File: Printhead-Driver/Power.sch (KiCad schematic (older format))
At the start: 50 parts, among them J3 24V Power In, J4 ADC Select1, U10 MC34063AD, U11 ADC121C021CIMM, U9 MCA1101-5-3

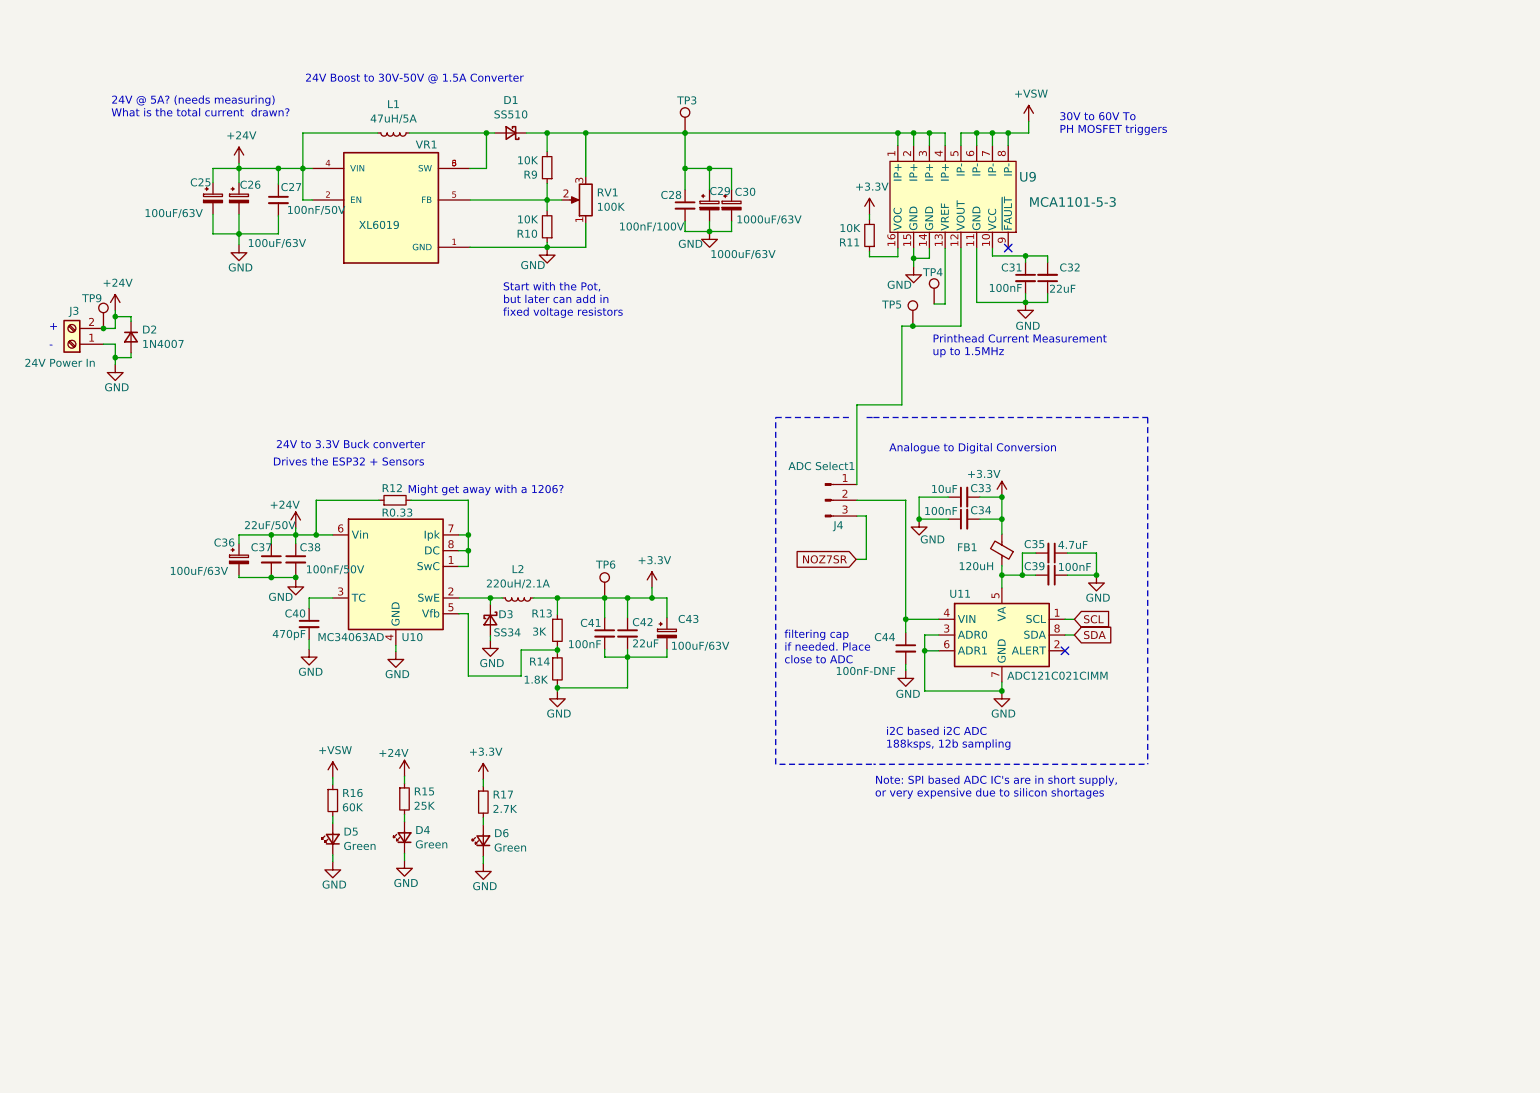
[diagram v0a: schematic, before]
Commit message: final PCB KiCAD design files for V0.5 as sent off for manufacture at JLCPCB 2022-03-22
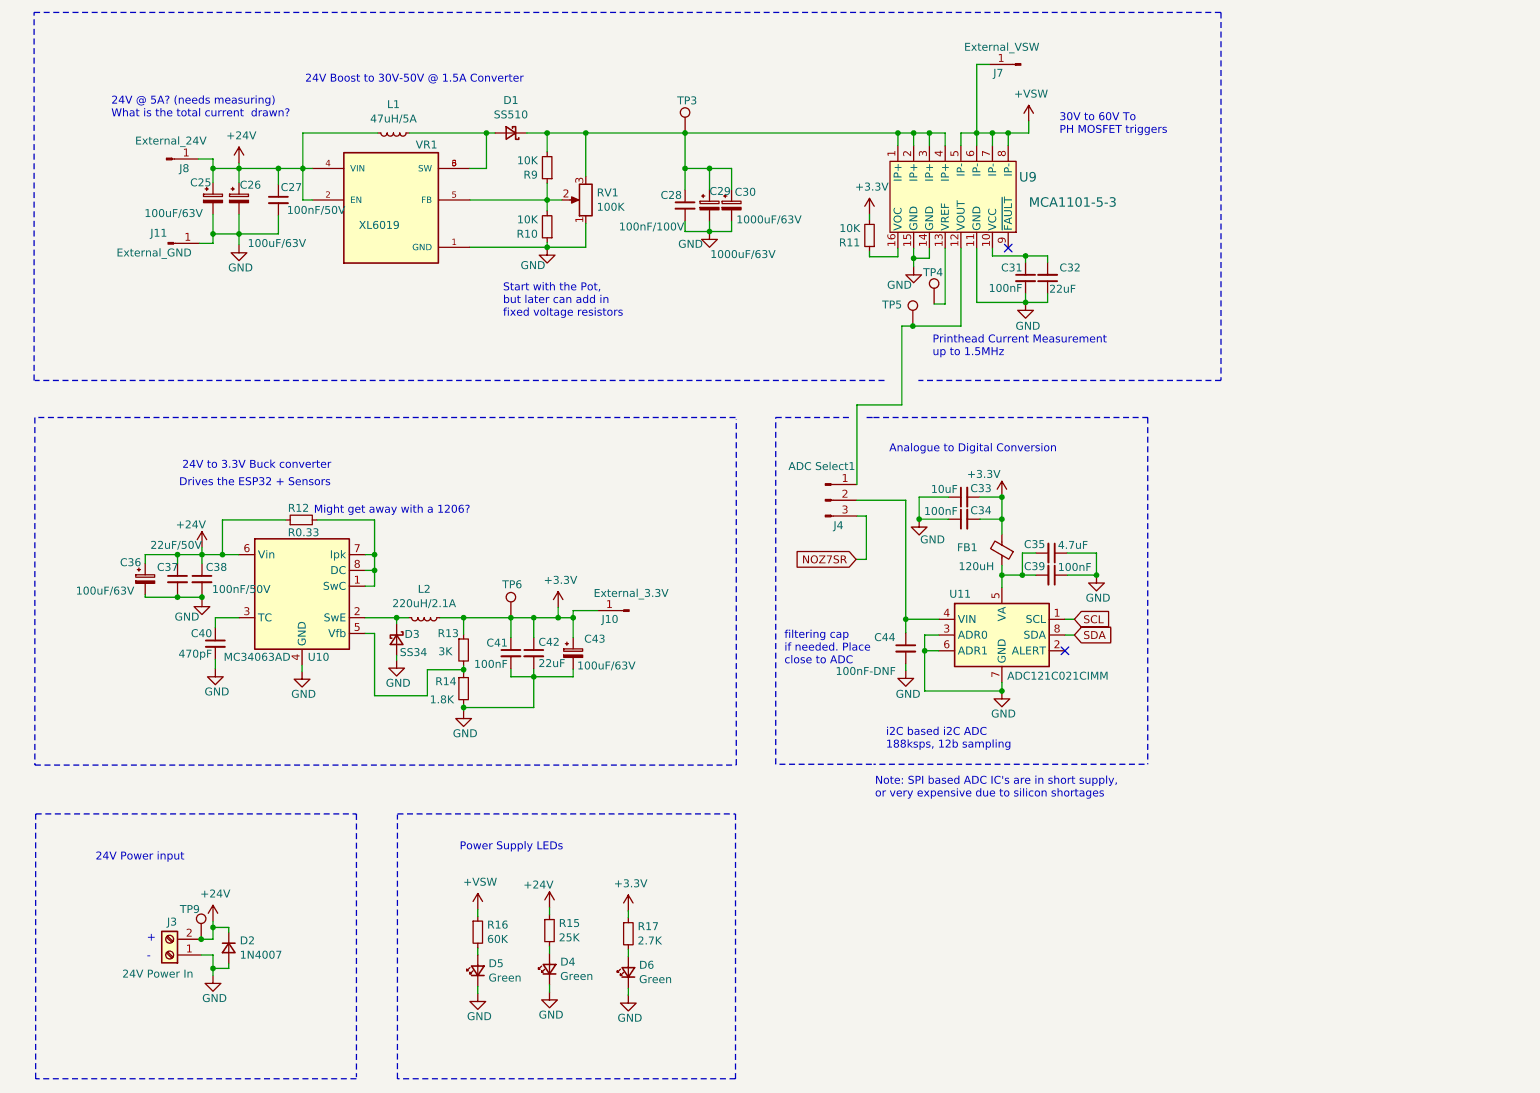
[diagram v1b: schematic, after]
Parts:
- added J10: External_3.3V, Connector_PinHeader_2.54mm:PinHeader_1x01_P2.54mm_Vertical, symbol Connector:Conn_01x01_Male
- added J11: External_GND, Connector_PinHeader_2.54mm:PinHeader_1x01_P2.54mm_Vertical, symbol Connector:Conn_01x01_Male
- added J7: External_VSW, Connector_PinHeader_2.54mm:PinHeader_1x01_P2.54mm_Vertical, symbol Connector:Conn_01x01_Male
- added J8: External_24V, Connector_PinHeader_2.54mm:PinHeader_1x01_P2.54mm_Vertical, symbol Connector:Conn_01x01_Male
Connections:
- net +24V: now also J8.1 (Pin_1)
- net +3V3: now also J10.1 (Pin_1)
- net +VSW: now also J7.1 (Pin_1)
- net GND: now also J11.1 (Pin_1)
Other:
- note added: "24V Power input"
- note added: "Power Supply LEDs"
- moved on the sheet: C36, C37, C38, C40, C41, C42, C43, D2, D3, D4, D5, D6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

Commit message: Adding in version 0.7 KiACD design files
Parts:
- removed C30: 1000uF/63V, Capacitor_THT:CP_Radial_D16.0mm_P7.50mm, symbol Device:CP_Small
- removed C31, C39: 100nF, Capacitor_SMD:C_0603_1608Metric, symbol Device:C_Small
- removed C32: 22uF, Capacitor_SMD:C_0603_1608Metric, symbol Device:C_Small
- removed D2: 1N4007, Diode_SMD:D_SMA, symbol Device:D_Small
- removed FB1: 120uH, Resistor_SMD:R_0805_2012Metric, symbol Device:Ferrite_Bead_Small
- removed J10: External_3.3V, Connector_PinHeader_2.54mm:PinHeader_1x01_P2.54mm_Vertical, symbol Connector:Conn_01x01_Male
- removed J11: External_GND, Connector_PinHeader_2.54mm:PinHeader_1x01_P2.54mm_Vertical, symbol Connector:Conn_01x01_Male
- removed J4: ADC Select1, Connector_PinHeader_2.54mm:PinHeader_1x03_P2.54mm_Vertical, symbol Connector:Conn_01x03_Male
- removed J7: External_VSW, Connector_PinHeader_2.54mm:PinHeader_1x01_P2.54mm_Vertical, symbol Connector:Conn_01x01_Male
- removed J8: External_24V, Connector_PinHeader_2.54mm:PinHeader_1x01_P2.54mm_Vertical, symbol Connector:Conn_01x01_Male
- removed TP4, TP5: TestPoint, TestPoint:TestPoint_THTPad_1.5x1.5mm_Drill0.7mm, symbol Connector:TestPoint
- removed U11: ADC121C021CIMM, Package_SO:MSOP-8_3x3mm_P0.65mm, symbol Analog_ADC:ADC121C021CIMM
- removed U9: MCA1101-5-3, Package_SO:SOIC-16W_7.5x10.3mm_P1.27mm, symbol Pauls_Symbol_Library:MCA1101-5-3
- added C36, C37, C51, C53, C55, C65, C67: 100nF, Capacitor_SMD:C_0603_1608Metric, symbol Device:C_Small
- added C38: 10nF/DNF, Capacitor_SMD:C_0603_1608Metric, symbol Device:C_Small
- added C45, C46, C47, C48, C49, C50: 1nF/DNF, Capacitor_SMD:C_0603_1608Metric, symbol Device:C_Small
- added C52, C54, C56, C66: 10uF, Capacitor_SMD:C_0603_1608Metric, symbol Device:C_Small
- added C61: 100nF 10V, Capacitor_SMD:C_0603_1608Metric, symbol Device:C_Small
- added C68: 1uF, Capacitor_SMD:C_0603_1608Metric, symbol Device:C_Small
- added D3: 12V, Diode_SMD:D_SOD-123, symbol Device:D_Zener_Small
- added D6: Green, Diode_SMD:D_0603_1608Metric, symbol Device:LED_Small
- added F1: 5A, Pauls_KiCAD_Libraries:Fuse_Holder_1808_10.0mmx5mm, symbol Device:Fuse_Small
- added L1, L4: 1uH 1.4A, Inductor_SMD:L_0805_2012Metric, symbol Device:L_Small
- added L3: 1uH 4A, Inductor_SMD:L_Taiyo-Yuden_MD-5050, symbol Device:L_Small
- added L6: 1uH/1.4A, Inductor_SMD:L_0805_2012Metric, symbol Device:L_Small
- added Q1, Q2: RU30L30, Pauls_KiCAD_Libraries:PDFN3333, symbol Pauls_Symbol_Library:RU30L30
- added R18: 4.7K, Resistor_SMD:R_0603_1608Metric, symbol Device:R_Small
- added R20, R24: 100k, Resistor_SMD:R_0603_1608Metric, symbol Device:R_Small
- added R21: 130, Resistor_SMD:R_0603_1608Metric, symbol Device:R_Small
- added R22: 150R, Resistor_SMD:R_0603_1608Metric, symbol Device:R_Small
- added R23: 100*, Resistor_SMD:R_0603_1608Metric, symbol Device:R_Small
- added R9: 100K, Resistor_SMD:R_0603_1608Metric, symbol Device:R_Small
- added SW1: PWR SW C128955, Pauls_KiCAD_Libraries:SW_SMD_SPDT_PCM12_7.8x3.8, symbol Pauls_Symbol_Library:Switch_Slide-3pole
- added TP10, TP11, TP12, TP6, TP8: TestPoint, TestPoint:TestPoint_THTPad_1.5x1.5mm_Drill0.7mm, symbol Connector:TestPoint
- added U17: ADC128S102CIMTX, Package_SO:TSSOP-16_4.4x5mm_P0.65mm, symbol Pauls_Symbol_Library:ADC128S102CIMTX
- added U18: HE6550MPR, Package_TO_SOT_SMD:SOT-89-3, symbol Pauls_Symbol_Library:HE6550MPR
- added U20: XC6227C331MR, Package_TO_SOT_SMD:SOT-23-5, symbol Printhead-Driver-rescue:XC6227C331MR-Pauls_Symbol_Library
- added U21: LM4040DIM3X-5, Package_TO_SOT_SMD:SOT-23, symbol Reference_Voltage:LM4040DBZ-5
- C33: value 10uF -> 1uF
- C35: value 4.7uF -> 1uF
- C41: renamed from C27; value 100nF/50V -> 100nF/100V
- C44: value 100nF-DNF -> 1nF/DNF; Description (none) -> 16V Ceramic
- C58: renamed from C37; value 22uF/50V -> 22uF/35V; footprint Capacitor_SMD:C_0603_1608Metric -> Capacitor_SMD:C_1210_3225Metric
- C59: renamed from C38; value 100nF/50V -> 100nF/35V; footprint Capacitor_SMD:C_0603_1608Metric -> Capacitor_SMD:C_1206_3216Metric
- C62: renamed from C41; value 100nF -> 100nF 10V
- D4, D5: footprint LED_SMD:LED_0805_2012Metric -> Diode_SMD:D_0603_1608Metric
- D7: renamed from D6; footprint LED_SMD:LED_0805_2012Metric -> Diode_SMD:D_0603_1608Metric
- J3: footprint TerminalBlock:TerminalBlock_Altech_AK300-2_P5.00mm -> Pauls_KiCAD_Libraries:JST-XH-2P_SMD
- R10: renamed from R9; value 10K -> 10K-DNF
- R12: renamed from R10; value 10K -> 10K-DNF
- R13: renamed from R12; footprint Resistor_SMD:R_2512_6332Metric -> Resistor_SMD:R_1206_3216Metric
- R14: renamed from R13; value 3K -> 4.7K
- R15: renamed from R14; value 1.8K -> 1.0K
- R16: renamed from R15; value 25K -> 27K; footprint Resistor_SMD:R_0805_2012Metric -> Resistor_SMD:R_0603_1608Metric
- R17: renamed from R16; value 60K -> 62K; footprint Resistor_SMD:R_0805_2012Metric -> Resistor_SMD:R_0603_1608Metric
- R19: renamed from R17; footprint Resistor_SMD:R_0805_2012Metric -> Resistor_SMD:R_0603_1608Metric
- renumbered C25 to C39, C26 to C40, C28 to C42, C29 to C43, C36 to C57, C40 to C60, C42 to C63, C43 to C64, D3 to D2, L1 to L2, L2 to L5, TP3 to TP5, TP6 to TP7, U10 to U19
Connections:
- net +24V: now also Q2.3 (D); no longer J3.2 (Pin_2), TP9.1
- net +3V3: now also C37.2, C65.1, C66.1, TP8.1, U17.13 (Vd+), U20.5 (VOUT); no longer C33.2, C34.2, C62.1, C63.1, C64.1, L5.1, R11.2, R14.1, TP7.1
- net +VSW: now also TP5.1, L3.1, R9.2
- net GND: now also C33.2, C34.2, C35.2, R11.1, C36.2, C37.1, C38.2, C45.2, C46.2, C47.2, C48.2, C49.2, C50.2, C51.2, C52.2, C53.2, C54.2, C55.2, C56.2, C61.2, C65.2, C66.2, C67.2, C68.2, D6.1 (K), R20.2, TP10.1, U17.12 (DGND), U17.3 (AGND), U18.1 (GND), U20.2 (GND), U21.2 (A); no longer C33.1, C34.1, C35.1
- net at C42.1, C43.1, D1.1 (K)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: now also L3.2; no longer TP5.1
- net at R14.2, U19.5 (Vfb): now also R22.1; no longer R15.1
- net NR1: now reaches C44.1
- net NR1: now also U17.5 (IN1)
- new net: C62.1, C63.1, L5.1, L6.2, R14.1, TP7.1
- new net: R15.1, R22.2
- new net: C36.1, R21.2, TP12.1, U17.2 (Va+), U21.1 (K)
- new net: C38.1, R23.2, U17.4 (IN0)
- new net: C53.1, C54.1, L4.1, U18.2 (VO)
- new net: D3.1 (K), Q1.1 (S), Q2.1 (S), R24.2
- new net: D3.2 (A), Q1.2 (G), R20.1, SW1.1
- new net: F1.2, Q1.3 (D)
- new net: F1.1, J3.2 (Pin_2), TP9.1
- new net: C35.1, L1.1, R21.1
- new net: Q2.2 (G), SW1.2
- new net: R24.1, SW1.3
- new net: D6.2 (A), R18.2
- new net +5V: C51.1, C52.1, L4.2, R18.1, TP6.1
- new net +6V: C33.1, C34.1, C55.1, C56.1, C61.1, C64.1, C67.1, C68.1, L1.2, L6.1, U18.3 (VI), U20.1 (VIN), U20.3 (CE)
- new net CS: U17.1 (~CS)
- new net MISO: U17.15 (MISO)
- new net MOSI: U17.14 (MOSI)
- new net NR2: C48.1, U17.6 (IN2)
- new net NR3: C45.1, U17.7 (IN3)
- new net NR4: C49.1, U17.8 (IN4)
- new net NR5: C46.1, U17.9 (IN5)
- new net NR6: C50.1, U17.10 (IN6)
- new net NR7: C47.1, U17.11 (IN7)
- new net SLCK: U17.16 (SCLK)
- new net VSW_Divider: R11.2, R23.1, R9.1, TP11.1
- no-connect marks 2 -> 0
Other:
- note added: "(when R15+R22 = 1200 Ohm)"
- note added: "* 1nF filter caps might \nneed to be larger?\nAdd 100 ohm resistors in series?"
- note added: "100KHz PWM Freq"
- note added: "188KHz PWM Freq"
- note added: "24V Boost to 25V-40V @ 4A Converter"
- note added: "24V to 6V Buck converter"
- note added: "45V = 4.091V\n40V = 3.636V\n35V = 3.182V\n30V = 2.727V\n24V = 2.182V"
- note added: "5V and 3.3V LDO Regulators"
- note added: "6.237V @1.2A"
- note added: "8 Channel 5V ADC"
- note added: "@150mA"
- note added: "@700mA"
- note added: "OFF"
- note added: "ON"
- note added: "Switched 24V Power input + Reverse Polarity Protection"
- note added: "Vout = 1.25 * (1+(R15+R22)/R14)"
- note removed: "24V @ 5A? (needs measuring)\nWhat is the total current drawn?"
- note removed: "24V Boost to 30V-50V @ 1.5A Converter"
- note removed: "24V Power input"
- note removed: "24V to 3.3V Buck converter"
- note removed: "30V to 60V To \nPH MOSFET triggers"
- note removed: "Analogue to Digital Conversion"
- note removed: "Might get away with a 1206?"
- note removed: "Note: SPI based ADC IC's are in short supply, \nor very expensive due to silicon shortages"
- note removed: "Printhead Current Measurement\nup to 1.5MHz"
- note removed: "filtering cap\nif needed. Place \nclose to ADC"
- note removed: "i2C based i2C ADC\n188ksps, 12b sampling"
- moved on the sheet: C39, C40, C41, C42, C43, C64, D1, D4, D5, D7, J3, L2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
